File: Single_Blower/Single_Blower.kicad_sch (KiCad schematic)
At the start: 14 parts, among them J1 BLOWER, J3 LED, J4 Sensor Connection, J5 LIMIT Switch, U2 5V

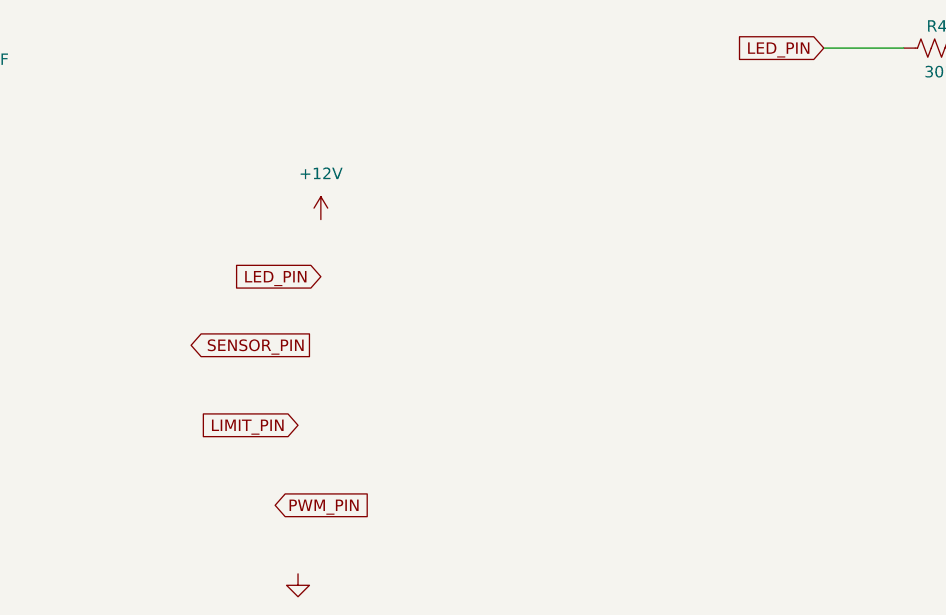
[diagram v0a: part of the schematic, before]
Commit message: Finished schematic on Blower card
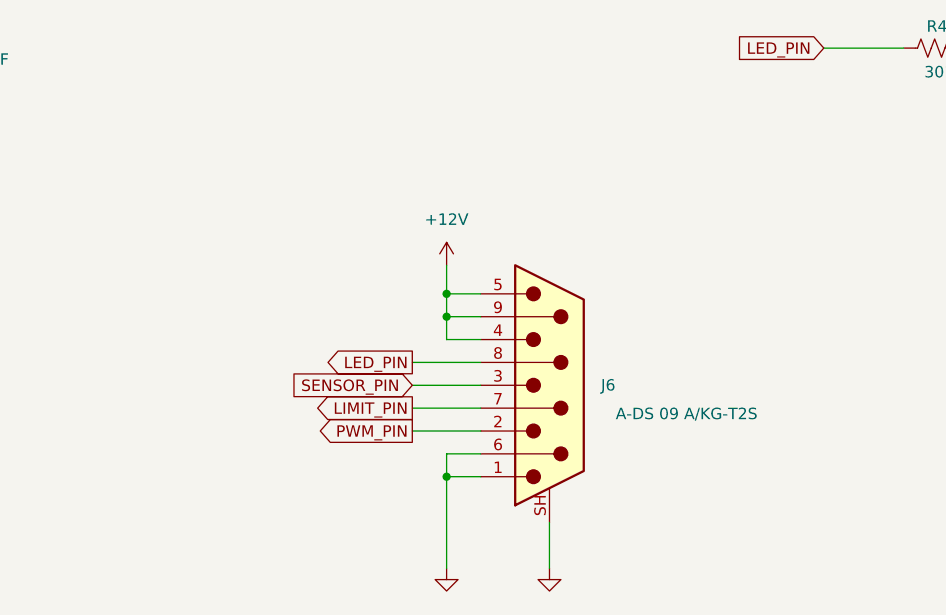
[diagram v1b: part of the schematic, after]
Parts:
- added J6: DE9_Pins_MountingHoles, Single_blower_footprints:ASSMANN_A-DS_09_A_KG-T2S, symbol Connector:DE9_Pins_MountingHoles
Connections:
- net +12V: now also J6.4, J6.5, J6.9
- net GND: now also J6.1, J6.6, J6.SH (PAD)
- net LED_PIN: now also J6.8
- net LIMIT_PIN: now also J6.7
- net PWM_PIN: now also J6.2
- net SENSOR_PIN: now also J6.3

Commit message: board layout
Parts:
- added D1: PWR, LED_SMD:LED_0805_2012Metric, symbol Device:LED
- added R3: 5.23k, Resistor_SMD:R_0805_2012Metric, symbol Device:R_US
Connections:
- net +12V: now also R3.1
- net GND: now also D1.1 (K)
- new net: D1.2 (A), R3.2
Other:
- moved on the sheet: C1, J6, R1, R2

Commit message: Beginning layout of the single blower
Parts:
- C1: footprint Switch_Daughter_Card_ftp:C0805 -> Capacitor_SMD:C_0805_2012Metric
- C15, C16, C2, C3: footprint Fan_Daughter_footprints:C0805 -> Capacitor_SMD:C_0805_2012Metric
- J1: footprint (none) -> Single_blower_footprints:TE_640457-4
- R1, R2: footprint Switch_Daughter_Card_ftp:R0805 -> Resistor_SMD:R_0805_2012Metric
- R4: footprint Fan_Daughter_footprints:R0805 -> Resistor_SMD:R_0805_2012Metric
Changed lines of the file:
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@@
 			)
 		)
-		(property "Footprint" "Switch_Daughter_Card_ftp:R0805"
+		(property "Footprint" "Resistor_SMD:R_0805_2012Metric"
 			(at 185.166 39.624 90)
 			(hide yes)
@@
 			)
 		)
-		(property "Footprint" "Switch_Daughter_Card_ftp:C0805"
+		(property "Footprint" "Capacitor_SMD:C_0805_2012Metric"
 			(at 172.72 52.07 0)
 			(hide yes)
@@
 			)
 		)
-		(property "Footprint" "Fan_Daughter_footprints:C0805"
+		(property "Footprint" "Capacitor_SMD:C_0805_2012Metric"
 			(at 52.07 44.45 0)
 			(hide yes)
@@
 			)
 		)
-		(property "Footprint" "Fan_Daughter_footprints:R0805"
+		(property "Footprint" "Resistor_SMD:R_0805_2012Metric"
 			(at 178.054 100.584 90)
 			(hide yes)
@@
 			)
 		)
-		(property "Footprint" "Switch_Daughter_Card_ftp:R0805"
+		(property "Footprint" "Resistor_SMD:R_0805_2012Metric"
 			(at 179.324 44.704 90)
 			(hide yes)
@@
 			)
 		)
-		(property "Footprint" "Fan_Daughter_footprints:C0805"
+		(property "Footprint" "Capacitor_SMD:C_0805_2012Metric"
 			(at 67.31 101.6 0)
 			(hide yes)
@@
 			)
 		)
-		(property "Footprint" "Fan_Daughter_footprints:C0805"
+		(property "Footprint" "Capacitor_SMD:C_0805_2012Metric"
 			(at 48.26 44.45 0)
 			(hide yes)
@@
 			)
 		)
-		(property "Footprint" "Fan_Daughter_footprints:C0805"
+		(property "Footprint" "Capacitor_SMD:C_0805_2012Metric"
 			(at 39.37 101.6 0)
 			(hide yes)
@@
 			)
 		)
-		(property "Footprint" ""
+		(property "Footprint" "Single_blower_footprints:TE_640457-4"
 			(at 29.21 33.02 0)
 			(hide yes)

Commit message: Finished routing single blower
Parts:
- added H1, H2, H3, H4: MountingHole, MountingHole:MountingHole_3.2mm_M3_DIN965, symbol Mechanical:MountingHole
- J3: footprint Single_blower_footprints:PHOENIX_1923759 -> Single_blower_footprints:TE_640457-2; Distributor PN 277-14388-ND -> A1926-ND; Mfg. Phoenix Contact -> TE Connectivity AMP Connectors; Mfg. PN 1923759 -> 640457-2
